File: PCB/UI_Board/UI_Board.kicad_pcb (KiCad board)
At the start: 2 copper layers, 149.4 x 35 mm, 14 parts, among them J1 DISPLAY, J2 CABLE, SW1 SW_UP, SW2 SW_DWN, SW3 SW_PRE_1, SW4 SW_PRE_2

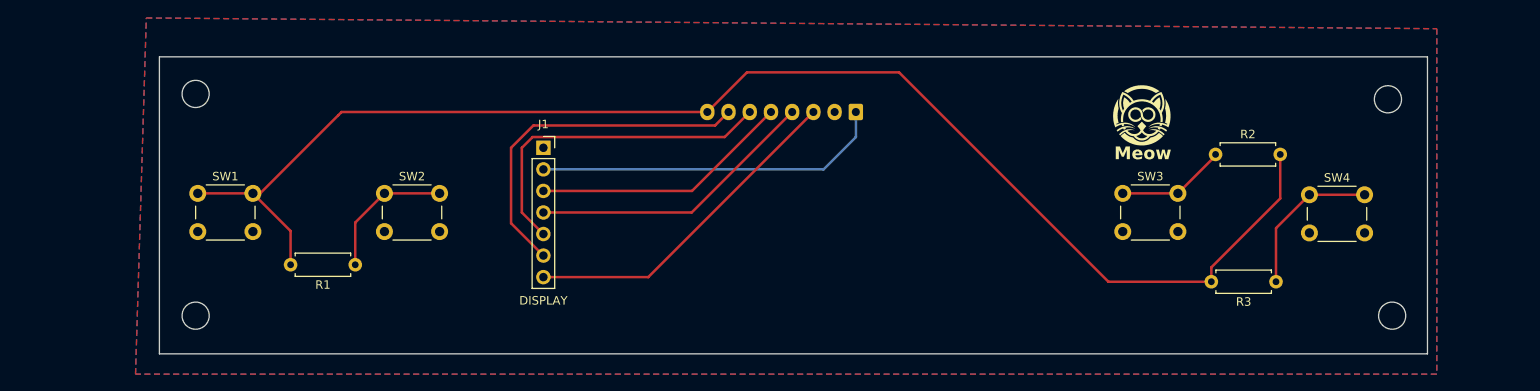
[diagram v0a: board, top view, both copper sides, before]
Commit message: chore: update UI board files and add build script
Update UI board KiCad project, schematic, and PCB. Add manufacturing
outputs (PDF, STEP, BOM). Add TFT display STEP model. Add
build_esp32s3.ps1 helper script for building under Windows PowerShell
without the IDF export.ps1 (works around MSYSTEM/py env mismatch).

Co-Authored-By: Claude Sonnet 4.6 <noreply@anthropic.com>
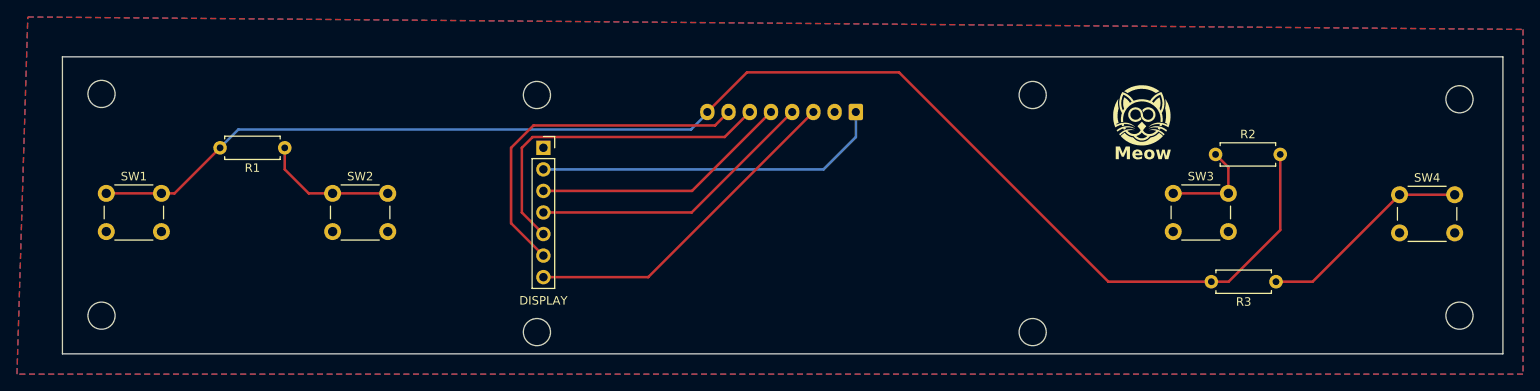
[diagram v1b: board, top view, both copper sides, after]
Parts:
- added H5: MountingHole, MountingHole:MountingHole_3.2mm_M3, F.Cu at (151.6, 39.5)
- added H6: MountingHole, MountingHole:MountingHole_3.2mm_M3, F.Cu at (151.6, 67.4)
- added H7: MountingHole, MountingHole:MountingHole_3.2mm_M3, F.Cu at (93.2, 67.4)
- added H8: MountingHole, MountingHole:MountingHole_3.2mm_M3, F.Cu at (93.2, 39.5)
- moved R1 16.1 mm to (63.5, 45.7)
- moved H2 11.1 mm to (41.9, 39.4)
- moved H4 11.1 mm to (41.9, 65.5)
- moved SW1 10.8 mm to (42.5, 51.1)
- moved SW4 10.6 mm to (194.9, 51.2)
- moved H1 8.43 mm to (201.9, 40.0)
- moved H3 7.93 mm to (201.9, 65.5)
- moved SW2 6.11 mm to (69.1, 51.1)
- moved SW3 5.95 mm to (168.2, 51.1)
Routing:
- net Net-(R3-Pad1): track 18.4 -> 25.3 mm
- net /BTNS: track 164.8 -> 167.5 mm
- net Net-(R2-Pad1): track 12.9 -> 11.9 mm
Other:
- board size 149.4 x 35 mm -> 169.8 x 35 mm
